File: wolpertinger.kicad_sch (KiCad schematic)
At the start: 80 parts, among them J1 RIGHT IN, J2 LEFT IN, J3 LEFT IN, J4 LEFT IN, J5 Jack-DC, K1 FRT5, K2 FRT5, Q1 BC549, SW1 ON/OFF, U1 4093, U2 TL074, U3 TL074, U4 VTL5C, U5 VTL5C, U6 VTL5C, U7 VTL5C, U8 TL072, U9 L78L05_TO92

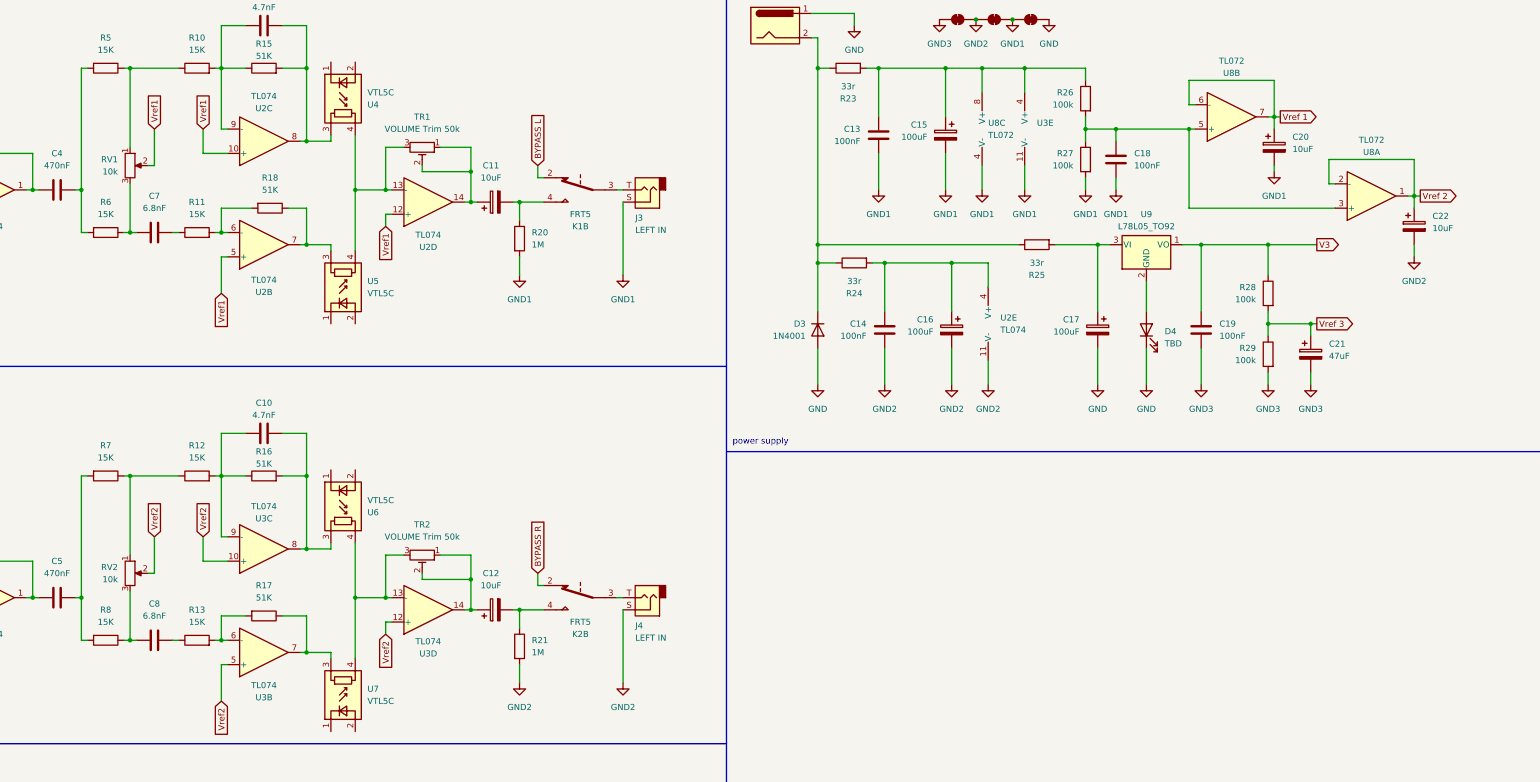
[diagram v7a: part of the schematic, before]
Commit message: Add internal LFO
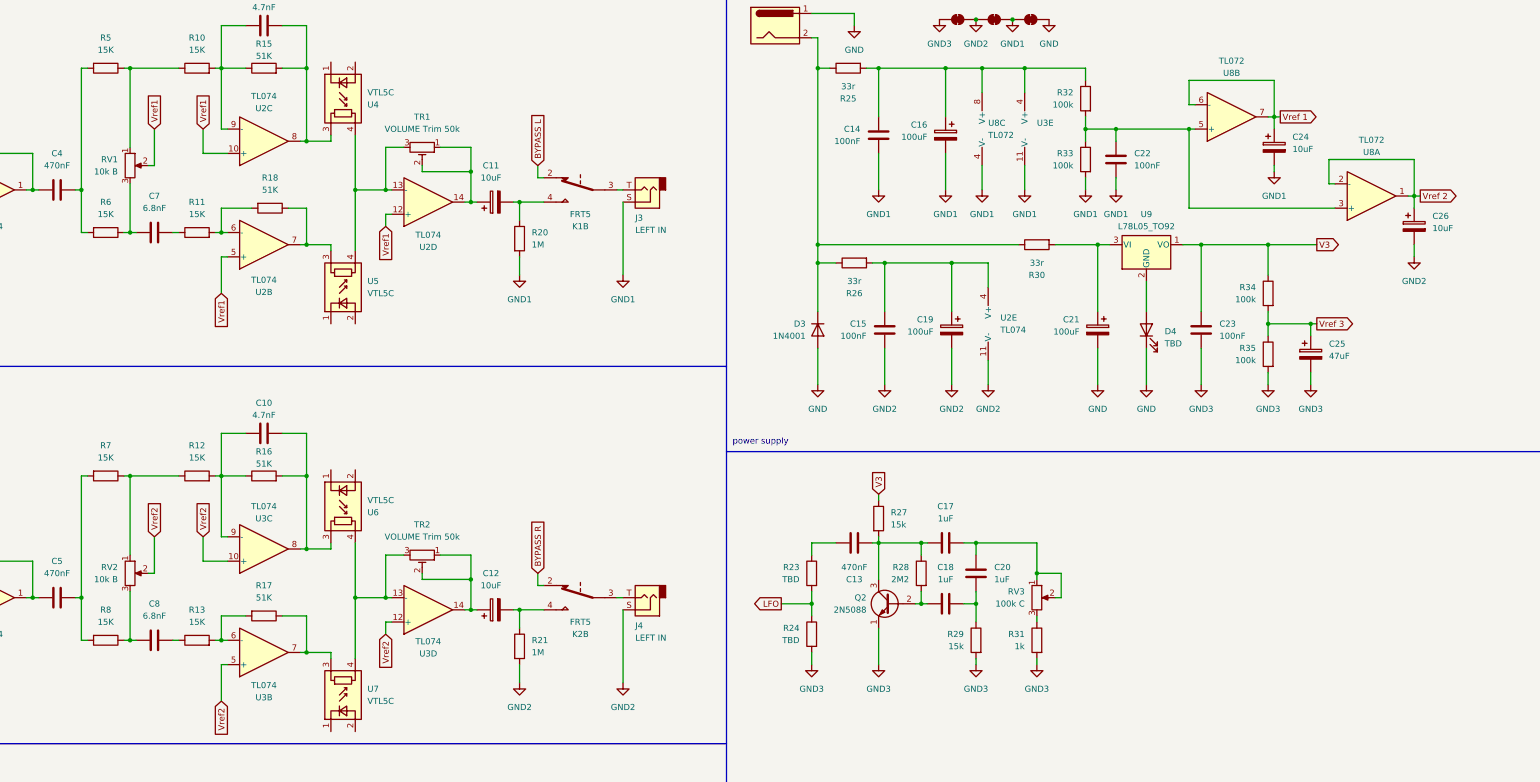
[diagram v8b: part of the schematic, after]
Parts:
- added C13: 470nF, symbol Device:C
- added C17, C18, C20: 1uF, symbol Device:C
- added Q2: 2N5088, Package_TO_SOT_THT:TO-92_Inline, symbol Device:Q_NPN
- added R23, R24: TBD, Resistor_THT:R_Axial_DIN0207_L6.3mm_D2.5mm_P7.62mm_Horizontal, symbol Device:R
- added R27, R29: 15k, Resistor_THT:R_Axial_DIN0207_L6.3mm_D2.5mm_P7.62mm_Horizontal, symbol Device:R
- added R28: 2M2, Resistor_THT:R_Axial_DIN0207_L6.3mm_D2.5mm_P7.62mm_Horizontal, symbol Device:R
- added R31: 1k, Resistor_THT:R_Axial_DIN0207_L6.3mm_D2.5mm_P7.62mm_Horizontal, symbol Device:R
- added RV3: 100k C, symbol Device:R_Potentiometer
- RV1, RV2: value 10k -> 10k B
- renumbered C13 to C14, C14 to C15, C15 to C16, C16 to C19, C17 to C21, C18 to C22, C19 to C23, C20 to C24, C21 to C25, C22 to C26, R23 to R25, R24 to R26, R25 to R30, R26 to R32, R27 to R33, R28 to R34, R29 to R35
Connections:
- net GND3: now also Q2.1 (E), R24.2, R29.2, R31.2
- net V3: now also R27.1
- new net: C13.1, C17.1, Q2.3 (C), R27.2, R28.1
- new net: C18.1, Q2.2 (B), R28.2
- new net: C17.2, C20.2, RV3.1, RV3.2
- new net: R31.1, RV3.3
- new net: C13.2, R23.1
- new net: C18.2, C20.1, R29.1
- new net LFO: R23.2, R24.1
